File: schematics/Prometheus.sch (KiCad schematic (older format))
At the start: 15 parts, among them J1 ATX Power Conn, SW2 Power Switch, U1 wdc65c816, U2 DS1501YN, X1 8MHz, X2 32kHz

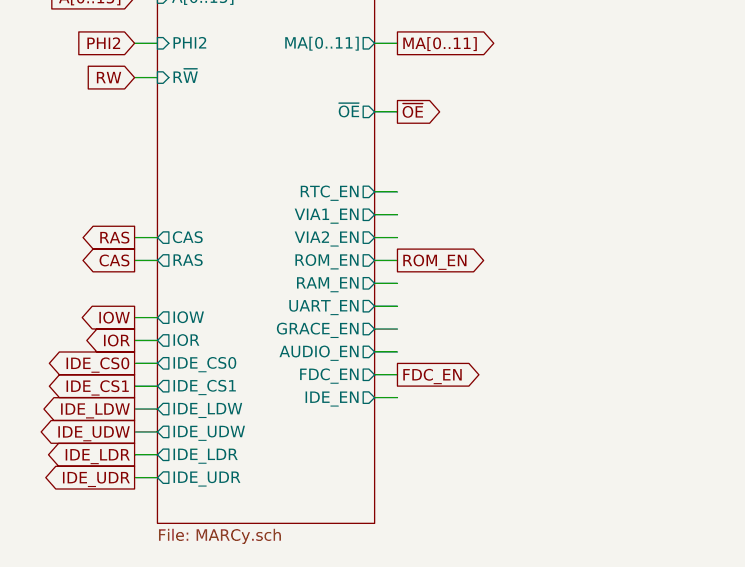
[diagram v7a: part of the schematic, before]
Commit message: Issue #4: Remove RAM_EN pin
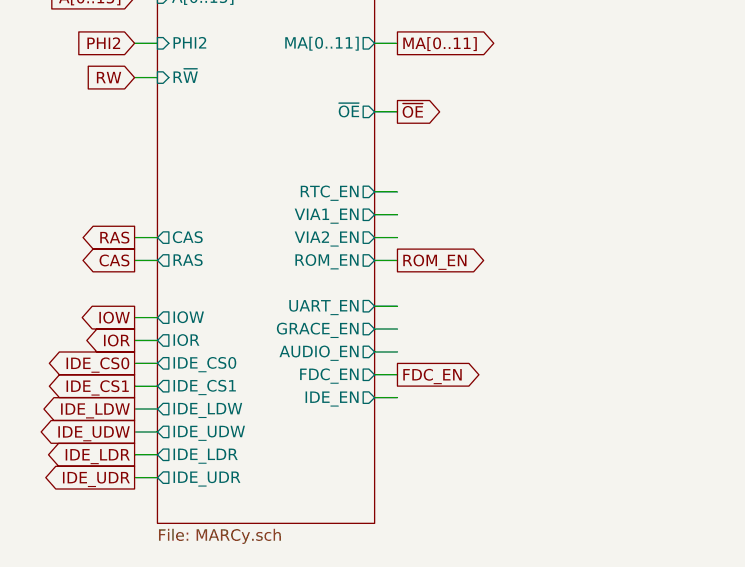
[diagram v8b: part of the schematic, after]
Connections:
- wire segments 184 -> 183
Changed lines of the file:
@@
 F8 "VIA2_EN" O R 2150 5950 50
 F9 "ROM_EN" O R 2150 6050 50
-F10 "RAM_EN" O R 2150 6150 50
-F11 "UART_EN" O R 2150 6250 50
-F12 "GRACE_EN" O R 2150 6350 50
-F13 "AUDIO_EN" O R 2150 6450 50
-F14 "FDC_EN" O R 2150 6550 50
-F15 "CAS" O L 1200 5950 50
-F16 "RAS" O L 1200 6050 50
-F17 "IDE_EN" O R 2150 6650 50
-F18 "IOW" O L 1200 6300 50
-F19 "IOR" O L 1200 6400 50
-F20 "IDE_CS1" O L 1200 6600 50
-F21 "IDE_CS0" O L 1200 6500 50
-F22 "IDE_UDW" O L 1200 6800 50
-F23 "IDE_LDW" O L 1200 6700 50
-F24 "IDE_UDR" O L 1200 7000 50
-F25 "IDE_LDR" O L 1200 6900 50
-F26 "GND" I R 2150 4750 50
-F27 "Vcc33" I R 2150 4850 50
-F28 "PHI2" I L 1200 5100 50
+F10 "UART_EN" O R 2150 6250 50
+F11 "GRACE_EN" O R 2150 6350 50
+F12 "AUDIO_EN" O R 2150 6450 50
+F13 "FDC_EN" O R 2150 6550 50
+F14 "CAS" O L 1200 5950 50
+F15 "RAS" O L 1200 6050 50
+F16 "IDE_EN" O R 2150 6650 50
+F17 "IOW" O L 1200 6300 50
+F18 "IOR" O L 1200 6400 50
+F19 "IDE_CS1" O L 1200 6600 50
+F20 "IDE_CS0" O L 1200 6500 50
+F21 "IDE_UDW" O L 1200 6800 50
+F22 "IDE_LDW" O L 1200 6700 50
+F23 "IDE_UDR" O L 1200 7000 50
+F24 "IDE_LDR" O L 1200 6900 50
+F25 "GND" I R 2150 4750 50
+F26 "Vcc33" I R 2150 4850 50
+F27 "PHI2" I L 1200 5100 50
 $EndSheet
 Text GLabel 1350 1550 2    50   Input ~ 0
@@
 	2150 6050 2250 6050
 Wire Wire Line
-	2150 6150 2250 6150
-Wire Wire Line
 	2150 6250 2250 6250
